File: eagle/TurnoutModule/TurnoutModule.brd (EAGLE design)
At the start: 61 x 48.3 mm, 19 parts, among them IC1 L293D, IC2 MCP23008/P

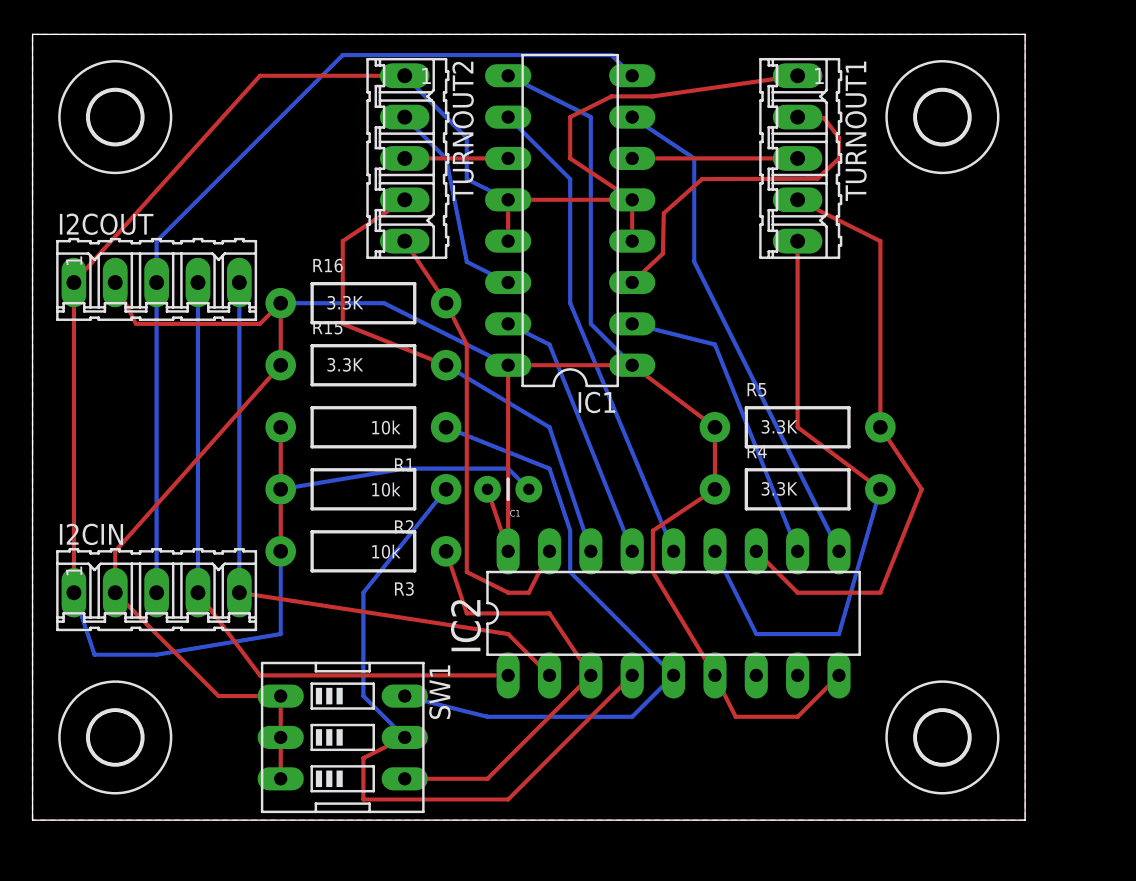
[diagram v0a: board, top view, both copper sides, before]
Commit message: 1.  Cleanup continues.  BlockController and the corresponding controller are deprecated along with SignalController and it's controller board.  These are replaced by the InputModule and OutputModule respectively 2.  TurnoutHandler moved to the MultiModuleController project folder 3.  Module moved to the MultiModuleController project folder 4.  More database cleanup work completed.
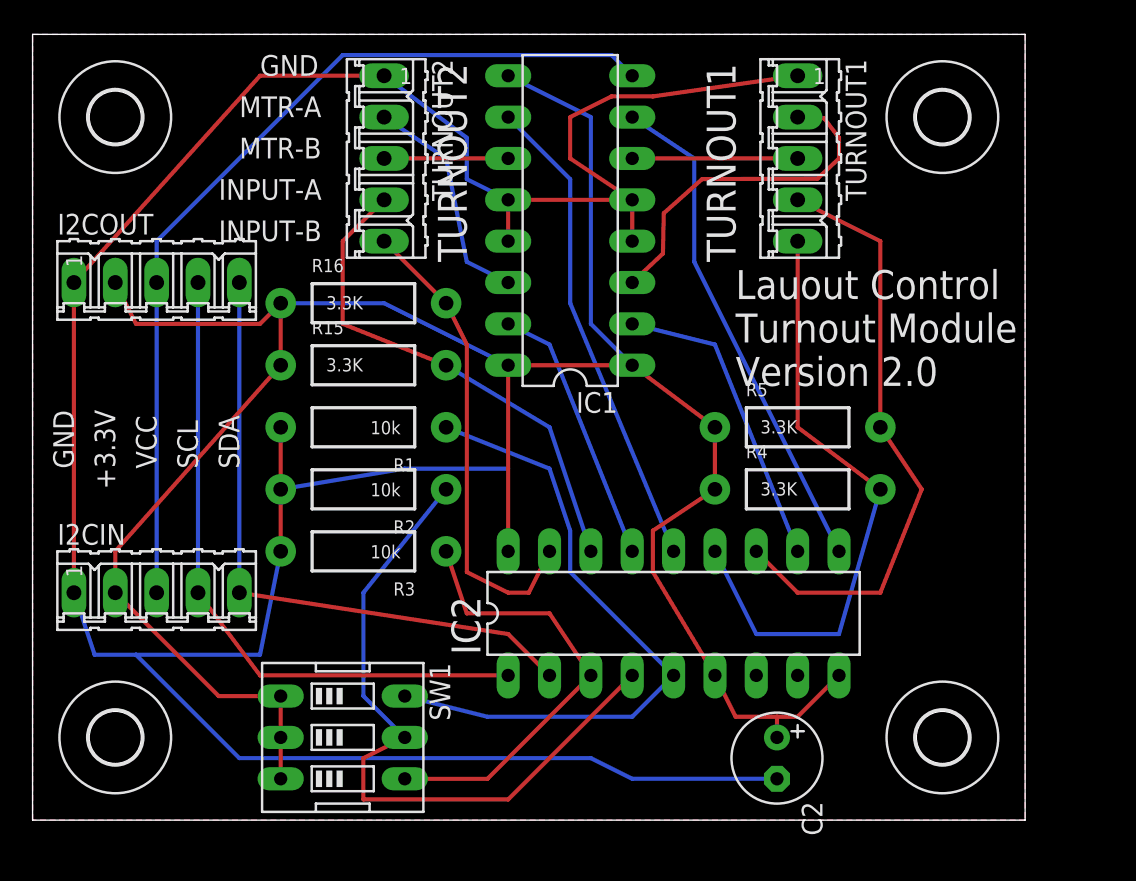
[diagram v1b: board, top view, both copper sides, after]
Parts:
- removed C1: 0.1uF, SparkFun-Capacitors:CAP-PTH-SMALL
- added C2: 10uf, rcl:E2,5-6
- I2CIN, I2COUT, TURNOUT1, TURNOUT2: value PIN1 -> PIN0
- moved TURNOUT2 1.27 mm to (21.6, 40.6)
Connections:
- net +3V3: now also C2.+; no longer C1.2
- net GND: now also C2.-; no longer C1.1
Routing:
- net GND: track 134.1 -> 174.3 mm
- net +3V3: track 146.6 -> 143.9 mm
- net N$13: track 6.35 -> 7.62 mm
- net N$5: track 31.9 -> 30.9 mm
- net N$10: track 12.9 -> 13.9 mm
- net N$2: track 28.3 -> 29.1 mm
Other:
- board text added: "+3.3V"
- board text added: "GND"
- board text added: "INPUT-A"
- board text added: "INPUT-B"
- board text added: "Lauout Control Turnout Module Version 2.0"
- board text added: "MTR-A"
- board text added: "MTR-B"
- board text added: "SCL"
- board text added: "SDA"
- board text added: "TURNOUT1"
- board text added: "TURNOUT2"
- board text added: "VCC"
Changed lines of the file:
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@@
 <wire x1="60.96" y1="48.26" x2="0" y2="48.26" width="0" layer="20"/>
 <wire x1="0" y1="48.26" x2="0" y2="0" width="0" layer="20"/>
+<text x="43.18" y="34.29" size="1.778" layer="21" rot="R90">TURNOUT1</text>
+<text x="26.67" y="34.29" size="1.778" layer="21" rot="R90">TURNOUT2</text>
+<text x="13.97" y="45.72" size="1.27" layer="21">GND</text>
+<text x="12.7" y="43.18" size="1.27" layer="21">MTR-A</text>
+<text x="12.7" y="40.64" size="1.27" layer="21">MTR-B</text>
+<text x="11.43" y="38.1" size="1.27" layer="21">INPUT-A</text>
+<text x="11.43" y="35.56" size="1.27" layer="21">INPUT-B</text>
+<text x="2.54" y="21.59" size="1.27" layer="21" rot="R90">GND</text>
+<text x="5.08" y="20.32" size="1.27" layer="21" rot="R90">+3.3V</text>
+<text x="7.62" y="21.59" size="1.27" layer="21" rot="R90">VCC</text>
+<text x="10.16" y="21.59" size="1.27" layer="21" rot="R90">SCL</text>
+<text x="12.7" y="21.59" size="1.27" layer="21" rot="R90">SDA</text>
+<text x="43.18" y="26.67" size="1.778" layer="21">Lauout Control
+Turnout Module
+Version 2.0</text>
 </plain>
 <attributes>
@@
 <element name="R4" library="SparkFun-Resistors" package="AXIAL-0.4" value="3.3K" x="46.99" y="20.32"/>
 <element name="R5" library="SparkFun-Resistors" package="AXIAL-0.4" value="3.3K" x="46.99" y="24.13"/>
-<element name="TURNOUT1" library="con-amp-quick" package="05P" value="PIN1" x="46.99" y="40.64" rot="R270">
+<element name="TURNOUT1" library="con-amp-quick" package="05P" value="PIN0" x="46.99" y="40.64" rot="R270">
 <attribute name="OC_FARNELL" value="unknown" x="46.99" y="40.64" size="1.778" layer="27" rot="R270" display="off"/>
 <attribute name="OC_NEWARK" value="unknown" x="46.99" y="40.64" size="1.778" layer="27" rot="R270" display="off"/>
@@
 <attribute name="MF" value="" x="46.99" y="40.64" size="1.778" layer="27" rot="R270" display="off"/>
 </element>
-<element name="TURNOUT2" library="con-amp-quick" package="05P" value="PIN1" x="22.86" y="40.64" rot="R270">
-<attribute name="OC_FARNELL" value="unknown" x="22.86" y="40.64" size="1.778" layer="27" rot="R270" display="off"/>
-<attribute name="OC_NEWARK" value="unknown" x="22.86" y="40.64" size="1.778" layer="27" rot="R270" display="off"/>
-<attribute name="MPN" value="" x="22.86" y="40.64" size="1.778" layer="27" rot="R270" display="off"/>
-<attribute name="MF" value="" x="22.86" y="40.64" size="1.778" layer="27" rot="R270" display="off"/>
+<element name="TURNOUT2" library="con-amp-quick" package="05P" value="PIN0" x="21.59" y="40.64" rot="R270">
+<attribute name="OC_FARNELL" value="unknown" x="21.59" y="40.64" size="1.778" layer="27" rot="R270" display="off"/>
+<attribute name="OC_NEWARK" value="unknown" x="21.59" y="40.64" size="1.778" layer="27" rot="R270" display="off"/>
+<attribute name="MPN" value="" x="21.59" y="40.64" size="1.778" layer="27" rot="R270" display="off"/>
+<attribute name="MF" value="" x="21.59" y="40.64" size="1.778" layer="27" rot="R270" display="off"/>
 </element>
 <element name="U$2" library="holes" package="3,2" value="" x="5.08" y="43.18"/>
@@
 <element name="U$5" library="holes" package="3,2" value="" x="55.88" y="5.08"/>
 <element name="IC2" library="adafruit" package="DIL18" value="MCP23008/P" x="39.37" y="12.7"/>
-<element name="I2COUT" library="con-amp-quick" package="05P" value="PIN1" x="7.62" y="33.02">
+<element name="I2COUT" library="con-amp-quick" package="05P" value="PIN0" x="7.62" y="33.02">
 <attribute name="MPN" value="" x="7.62" y="33.02" size="1.778" layer="27" display="off"/>
 <attribute name="OC_FARNELL" value="unknown" x="7.62" y="33.02" size="1.778" layer="27" display="off"/>
@@
 <attribute name="OC_NEWARK" value="unknown" x="7.62" y="33.02" size="1.778" layer="27" display="off"/>
 </element>
-<element name="I2CIN" library="con-amp-quick" package="05P" value="PIN1" x="7.62" y="13.97">
+<element name="I2CIN" library="con-amp-quick" package="05P" value="PIN0" x="7.62" y="13.97">
 <attribute name="MPN" value="" x="7.62" y="13.97" size="1.778" layer="27" display="off"/>
 <attribute name="OC_FARNELL" value="unknown" x="7.62" y="13.97" size="1.778" layer="27" display="off"/>
@@
 <attribute name="OC_NEWARK" value="unknown" x="7.62" y="13.97" size="1.778" layer="27" display="off"/>
 </element>
-<element name="C1" library="SparkFun-Capacitors" package="CAP-PTH-SMALL" value="0.1uF" x="30.48" y="20.32" rot="R180"/>
 <element name="R1" library="SparkFun-Resistors" package="AXIAL-0.4" value="10k" x="20.32" y="24.13" rot="R180"/>
 <element name="R2" library="SparkFun-Resistors" package="AXIAL-0.4" value="10k" x="20.32" y="20.32" rot="R180"/>
 <element name="R3" library="SparkFun-Resistors" package="AXIAL-0.4" value="10k" x="20.32" y="16.51" rot="R180"/>
 <element name="SW1" library="special" package="EDG-03" value="" x="19.05" y="5.08" rot="R270"/>
+<element name="C2" library="rcl" package="E2,5-6" value="10uf" x="45.72" y="3.81" rot="R270"/>
 </elements>
 <signals>
@@
 <wire x1="2.54" y1="13.97" x2="2.54" y2="33.02" width="0.254" layer="1"/>
 <wire x1="2.54" y1="33.02" x2="13.97" y2="45.72" width="0.254" layer="1"/>
-<wire x1="13.97" y1="45.72" x2="22.86" y2="45.72" width="0.254" layer="1"/>
+<wire x1="13.97" y1="45.72" x2="21.59" y2="45.72" width="0.254" layer="1"/>
 <wire x1="36.83" y1="38.1" x2="29.21" y2="38.1" width="0.254" layer="1"/>
 <wire x1="46.99" y1="45.72" x2="38.1" y2="44.45" width="0.254" layer="1"/>
@@
 <wire x1="33.02" y1="43.18" x2="33.02" y2="40.64" width="0.254" layer="1"/>
 <wire x1="33.02" y1="40.64" x2="36.83" y2="38.1" width="0.254" layer="1"/>
-<wire x1="22.86" y1="45.72" x2="26.67" y2="41.91" width="0.254" layer="16"/>
+<wire x1="21.59" y1="45.72" x2="26.67" y2="41.91" width="0.254" layer="16"/>
 <wire x1="29.21" y1="38.1" x2="26.67" y2="39.37" width="0.254" layer="16"/>
 <wire x1="26.67" y1="39.37" x2="26.67" y2="41.91" width="0.254" layer="16"/>
-<contactref element="C1" pad="1"/>
 <contactref element="R3" pad="P$2"/>
 <contactref element="R1" pad="P$2"/>
@@
 <wire x1="15.24" y1="16.51" x2="15.24" y2="20.32" width="0.254" layer="1"/>
 <wire x1="15.24" y1="20.32" x2="15.24" y2="24.13" width="0.254" layer="1"/>
-<wire x1="15.24" y1="16.51" x2="15.24" y2="11.43" width="0.254" layer="16"/>
-<wire x1="15.24" y1="11.43" x2="7.62" y2="10.16" width="0.254" layer="16"/>
-<wire x1="7.62" y1="10.16" x2="3.81" y2="10.16" width="0.254" layer="16"/>
+<wire x1="15.24" y1="16.51" x2="13.97" y2="10.16" width="0.254" layer="16"/>
+<wire x1="13.97" y1="10.16" x2="6.35" y2="10.16" width="0.254" layer="16"/>
+<wire x1="6.35" y1="10.16" x2="3.81" y2="10.16" width="0.254" layer="16"/>
 <wire x1="3.81" y1="10.16" x2="2.54" y2="13.97" width="0.254" layer="16"/>
 <wire x1="15.24" y1="20.32" x2="22.86" y2="21.59" width="0.254" layer="16"/>
 <wire x1="22.86" y1="21.59" x2="29.21" y2="21.59" width="0.254" layer="16"/>
-<wire x1="29.21" y1="21.59" x2="30.48" y2="20.32" width="0.254" layer="16"/>
 <polygon width="0.254" layer="1" isolate="0.3048">
 <vertex x="0" y="0"/>
@@
 <vertex x="60.96" y="0"/>
 </polygon>
+<contactref element="C2" pad="-"/>
+<wire x1="45.72" y1="2.54" x2="36.83" y2="2.54" width="0.254" layer="16"/>
+<wire x1="36.83" y1="2.54" x2="34.29" y2="3.81" width="0.254" layer="16"/>
+<wire x1="34.29" y1="3.81" x2="12.7" y2="3.81" width="0.254" layer="16"/>
+<wire x1="12.7" y1="3.81" x2="6.35" y2="10.16" width="0.254" layer="16"/>
 </signal>
 <signal name="N$29">
@@
 <contactref element="R16" pad="P$2"/>
 <contactref element="IC2" pad="17"/>
-<wire x1="25.4" y1="31.75" x2="22.86" y2="35.56" width="0.254" layer="1"/>
+<wire x1="25.4" y1="31.75" x2="21.59" y2="35.56" width="0.254" layer="1"/>
 <wire x1="25.4" y1="31.75" x2="26.67" y2="29.21" width="0.254" layer="1"/>
 <wire x1="26.67" y1="29.21" x2="26.67" y2="15.24" width="0.254" layer="1"/>
@@
 <wire x1="25.4" y1="27.94" x2="19.05" y2="30.48" width="0.254" layer="1"/>
 <wire x1="19.05" y1="30.48" x2="19.05" y2="35.56" width="0.254" layer="1"/>
-<wire x1="19.05" y1="35.56" x2="22.86" y2="38.1" width="0.254" layer="1"/>
+<wire x1="19.05" y1="35.56" x2="21.59" y2="38.1" width="0.254" layer="1"/>
 </signal>
 <signal name="N$6">
@@
 <wire x1="29.21" y1="33.02" x2="26.67" y2="34.29" width="0.254" layer="16"/>
 <wire x1="26.67" y1="34.29" x2="25.4" y2="40.64" width="0.254" layer="16"/>
-<wire x1="25.4" y1="40.64" x2="22.86" y2="43.18" width="0.254" layer="16"/>
+<wire x1="25.4" y1="40.64" x2="21.59" y2="43.18" width="0.254" layer="16"/>
 </signal>
 <signal name="N$13">
 <contactref element="TURNOUT2" pad="3"/>
 <contactref element="IC1" pad="11"/>
-<wire x1="29.21" y1="40.64" x2="22.86" y2="40.64" width="0.254" layer="1"/>
+<wire x1="29.21" y1="40.64" x2="21.59" y2="40.64" width="0.254" layer="1"/>
 </signal>
 <signal name="N$15">
@@
 <wire x1="38.1" y1="15.24" x2="38.1" y2="17.78" width="0.254" layer="1"/>
 <wire x1="38.1" y1="17.78" x2="41.91" y2="20.32" width="0.254" layer="1"/>
-<contactref element="C1" pad="2"/>
-<wire x1="27.94" y1="20.32" x2="29.21" y2="16.51" width="0.254" layer="1"/>
 <wire x1="15.24" y1="31.75" x2="13.97" y2="30.48" width="0.254" layer="1"/>
 <wire x1="13.97" y1="30.48" x2="6.35" y2="30.48" width="0.254" layer="1"/>
@@
 <wire x1="11.43" y1="7.62" x2="5.08" y2="13.97" width="0.254" layer="1"/>
 <wire x1="41.91" y1="8.89" x2="43.18" y2="6.35" width="0.254" layer="1"/>
-<wire x1="43.18" y1="6.35" x2="46.99" y2="6.35" width="0.254" layer="1"/>
+<wire x1="43.18" y1="6.35" x2="45.72" y2="6.35" width="0.254" layer="1"/>
+<wire x1="45.72" y1="6.35" x2="46.99" y2="6.35" width="0.254" layer="1"/>
 <wire x1="46.99" y1="6.35" x2="49.53" y2="8.89" width="0.254" layer="1"/>
+<contactref element="C2" pad="+"/>
+<wire x1="45.72" y1="5.08" x2="45.72" y2="6.35" width="0.254" layer="1"/>
 </signal>
 <signal name="N$8">
@@
 </board>
 </drawing>
+<compatibility>
+<note version="6.3" minversion="6.2.2" severity="warning">
+Since Version 6.2.2 text objects can contain more than one line,
+which will not be processed correctly with this version.
+</note>
+</compatibility>
 </eagle>

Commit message: 1.  Cleanup work 2.  Reduced the retry timeout to 2 seconds (from 3) 3.  Change the TurnoutModule board to use the same address pins as the other modules 4.  Add a two-pin header to Input and Output module boards with access to GND and 3.3v 5.  Move the call to module->finishxxx to before network setup code so that the modules can initialize while the network connection is being established
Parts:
- renumbered TURNOUT1 to PORT0, TURNOUT2 to PORT1
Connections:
- net N$1: now also SW1.4; no longer SW1.6
- net N$7: now also SW1.6; no longer SW1.4
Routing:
- net N$4: track 43.1 -> 34.1 mm
- net N$7: track 27.7 -> 22.9 mm
- net N$1: track 40.1 -> 41.9 mm
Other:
- board text added: "PORT 0"
- board text added: "PORT 1"
- board text removed: "TURNOUT1"
- board text removed: "TURNOUT2"
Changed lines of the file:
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@@
 <wire x1="60.96" y1="48.26" x2="0" y2="48.26" width="0" layer="20"/>
 <wire x1="0" y1="48.26" x2="0" y2="0" width="0" layer="20"/>
-<text x="43.18" y="34.29" size="1.778" layer="21" rot="R90">TURNOUT1</text>
-<text x="26.67" y="34.29" size="1.778" layer="21" rot="R90">TURNOUT2</text>
+<text x="43.18" y="34.29" size="1.778" layer="21" rot="R90">PORT 0</text>
+<text x="26.67" y="34.29" size="1.778" layer="21" rot="R90">PORT 1</text>
 <text x="13.97" y="45.72" size="1.27" layer="21">GND</text>
 <text x="12.7" y="43.18" size="1.27" layer="21">MTR-A</text>
@@
 <element name="R4" library="SparkFun-Resistors" package="AXIAL-0.4" value="3.3K" x="46.99" y="20.32"/>
 <element name="R5" library="SparkFun-Resistors" package="AXIAL-0.4" value="3.3K" x="46.99" y="24.13"/>
-<element name="TURNOUT1" library="con-amp-quick" package="05P" value="PIN0" x="46.99" y="40.64" rot="R270">
+<element name="PORT0" library="con-amp-quick" package="05P" value="PIN0" x="46.99" y="40.64" rot="R270">
 <attribute name="OC_FARNELL" value="unknown" x="46.99" y="40.64" size="1.778" layer="27" rot="R270" display="off"/>
 <attribute name="OC_NEWARK" value="unknown" x="46.99" y="40.64" size="1.778" layer="27" rot="R270" display="off"/>
@@
 <attribute name="MF" value="" x="46.99" y="40.64" size="1.778" layer="27" rot="R270" display="off"/>
 </element>
-<element name="TURNOUT2" library="con-amp-quick" package="05P" value="PIN0" x="21.59" y="40.64" rot="R270">
+<element name="PORT1" library="con-amp-quick" package="05P" value="PIN0" x="21.59" y="40.64" rot="R270">
 <attribute name="OC_FARNELL" value="unknown" x="21.59" y="40.64" size="1.778" layer="27" rot="R270" display="off"/>
 <attribute name="OC_NEWARK" value="unknown" x="21.59" y="40.64" size="1.778" layer="27" rot="R270" display="off"/>
@@
 <signals>
 <signal name="GND">
-<contactref element="TURNOUT1" pad="1"/>
+<contactref element="PORT0" pad="1"/>
 <contactref element="IC1" pad="5"/>
 <contactref element="IC1" pad="4"/>
 <contactref element="IC1" pad="12"/>
 <contactref element="IC1" pad="13"/>
-<contactref element="TURNOUT2" pad="1"/>
+<contactref element="PORT1" pad="1"/>
 <wire x1="29.21" y1="38.1" x2="29.21" y2="35.56" width="0.254" layer="1"/>
 <wire x1="36.83" y1="35.56" x2="36.83" y2="38.1" width="0.254" layer="1"/>
@@
 </signal>
 <signal name="N$29">
-<contactref element="TURNOUT1" pad="5"/>
+<contactref element="PORT0" pad="5"/>
 <contactref element="R4" pad="P$2"/>
 <contactref element="IC2" pad="13"/>
@@
 </signal>
 <signal name="N$12">
-<contactref element="TURNOUT1" pad="4"/>
+<contactref element="PORT0" pad="4"/>
 <contactref element="R5" pad="P$2"/>
 <contactref element="IC2" pad="12"/>
@@
 </signal>
 <signal name="N$2">
-<contactref element="TURNOUT2" pad="5"/>
+<contactref element="PORT1" pad="5"/>
 <contactref element="R16" pad="P$2"/>
 <contactref element="IC2" pad="17"/>
@@
 </signal>
 <signal name="N$5">
-<contactref element="TURNOUT2" pad="4"/>
+<contactref element="PORT1" pad="4"/>
 <contactref element="R15" pad="P$2"/>
 <contactref element="IC2" pad="16"/>
@@
 </signal>
 <signal name="N$6">
-<contactref element="TURNOUT1" pad="3"/>
+<contactref element="PORT0" pad="3"/>
 <contactref element="IC1" pad="6"/>
 <wire x1="36.83" y1="40.64" x2="46.99" y2="40.64" width="0.254" layer="1"/>
@@
 </signal>
 <signal name="N$10">
-<contactref element="TURNOUT2" pad="2"/>
+<contactref element="PORT1" pad="2"/>
 <contactref element="IC1" pad="14"/>
 <wire x1="29.21" y1="33.02" x2="26.67" y2="34.29" width="0.254" layer="16"/>
@@
 </signal>
 <signal name="N$13">
-<contactref element="TURNOUT2" pad="3"/>
+<contactref element="PORT1" pad="3"/>
 <contactref element="IC1" pad="11"/>
 <wire x1="29.21" y1="40.64" x2="21.59" y2="40.64" width="0.254" layer="1"/>
@@
 </signal>
 <signal name="N$3">
-<contactref element="TURNOUT1" pad="2"/>
+<contactref element="PORT0" pad="2"/>
 <contactref element="IC1" pad="3"/>
 <wire x1="36.83" y1="33.02" x2="38.716428125" y2="34.79809375" width="0.254" layer="1"/>
@@
 <contactref element="R1" pad="P$1"/>
 <contactref element="IC2" pad="5"/>
-<contactref element="SW1" pad="6"/>
-<wire x1="22.86" y1="7.62" x2="27.94" y2="6.35" width="0.254" layer="16"/>
-<wire x1="27.94" y1="6.35" x2="36.83" y2="6.35" width="0.254" layer="16"/>
-<wire x1="36.83" y1="6.35" x2="39.37" y2="8.89" width="0.254" layer="16"/>
 <wire x1="25.4" y1="24.13" x2="31.75" y2="21.59" width="0.254" layer="16"/>
 <wire x1="31.75" y1="21.59" x2="33.02" y2="17.78" width="0.254" layer="16"/>
 <wire x1="33.02" y1="17.78" x2="33.02" y2="15.24" width="0.254" layer="16"/>
 <wire x1="33.02" y1="15.24" x2="39.37" y2="8.89" width="0.254" layer="16"/>
+<contactref element="SW1" pad="4"/>
+<wire x1="22.86" y1="2.54" x2="34.29" y2="2.54" width="0.254" layer="1"/>
+<wire x1="34.29" y1="2.54" x2="39.37" y2="8.89" width="0.254" layer="1"/>
 </signal>
 <signal name="N$4">
@@
 <contactref element="R2" pad="P$1"/>
 <contactref element="SW1" pad="5"/>
-<wire x1="22.86" y1="5.08" x2="20.32" y2="3.81" width="0.254" layer="1"/>
-<wire x1="20.32" y1="3.81" x2="20.32" y2="1.27" width="0.254" layer="1"/>
-<wire x1="20.32" y1="1.27" x2="29.21" y2="1.27" width="0.254" layer="1"/>
-<wire x1="29.21" y1="1.27" x2="36.83" y2="8.89" width="0.254" layer="1"/>
+<wire x1="22.86" y1="5.08" x2="34.29" y2="5.08" width="0.254" layer="1"/>
+<wire x1="34.29" y1="5.08" x2="35.56" y2="6.35" width="0.254" layer="1"/>
+<wire x1="35.56" y1="6.35" x2="36.83" y2="8.89" width="0.254" layer="1"/>
 <wire x1="25.4" y1="20.32" x2="20.32" y2="13.97" width="0.254" layer="16"/>
 <wire x1="20.32" y1="13.97" x2="20.32" y2="7.62" width="0.254" layer="16"/>
@@
 <contactref element="IC2" pad="3"/>
 <contactref element="R3" pad="P$1"/>
-<contactref element="SW1" pad="4"/>
-<wire x1="22.86" y1="2.54" x2="27.94" y2="2.54" width="0.254" layer="1"/>
-<wire x1="27.94" y1="2.54" x2="34.29" y2="8.89" width="0.254" layer="1"/>
 <wire x1="34.29" y1="8.89" x2="31.75" y2="12.7" width="0.254" layer="1"/>
 <wire x1="31.75" y1="12.7" x2="26.67" y2="12.7" width="0.254" layer="1"/>
 <wire x1="26.67" y1="12.7" x2="25.4" y2="16.51" width="0.254" layer="1"/>
+<contactref element="SW1" pad="6"/>
+<wire x1="22.86" y1="7.62" x2="25.4" y2="16.51" width="0.254" layer="16"/>
 </signal>
 </signals>
